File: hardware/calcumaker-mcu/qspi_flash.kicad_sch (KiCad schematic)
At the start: 3 parts, among them U7 W25Q32JVSSIQ

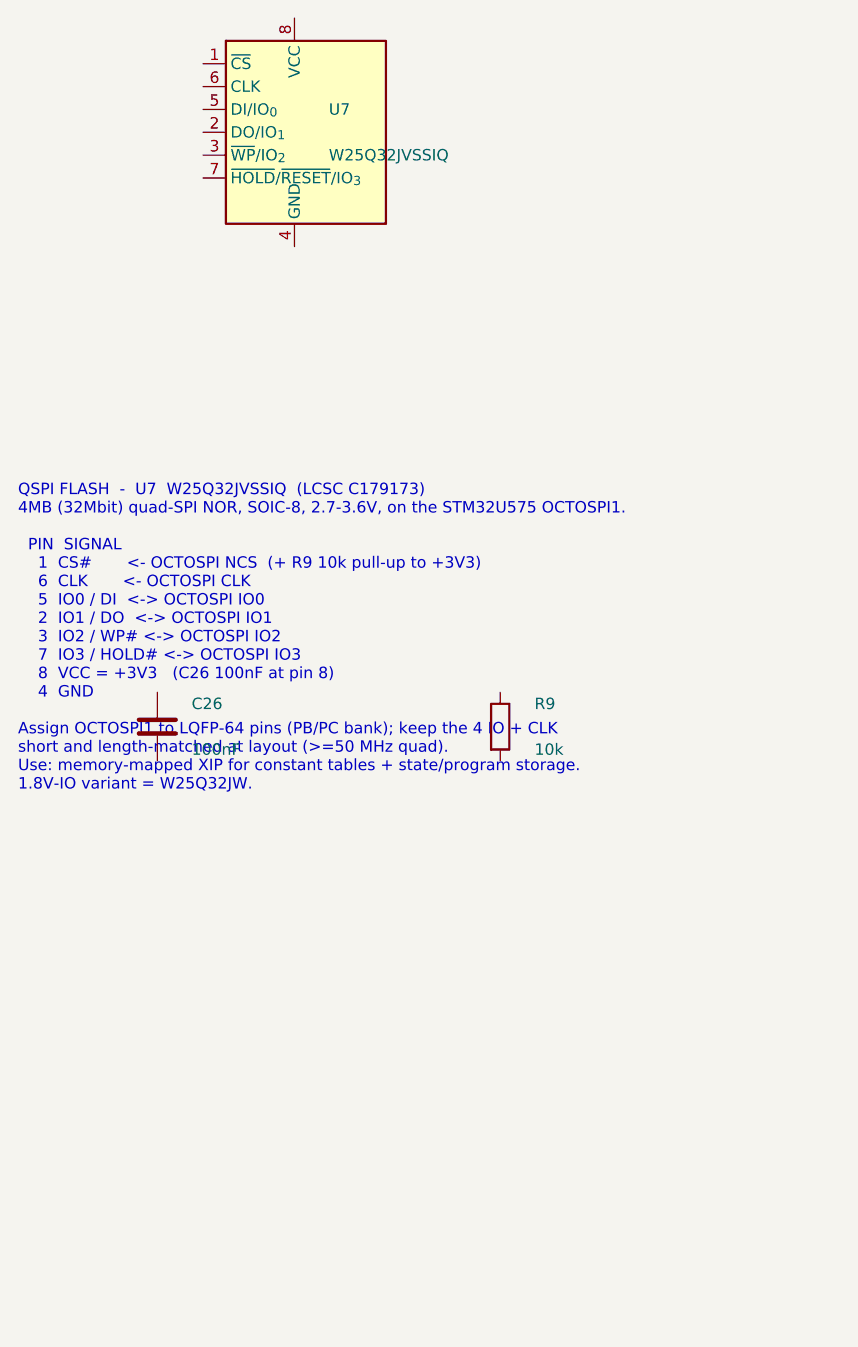
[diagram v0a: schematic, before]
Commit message: hardware: per-key RGB hint lighting on the keyboard board (50x SK6805 on gated VSYS) (#4)
Add addressable RGB accent lighting that hints key positions / presses -- one
SK6805-EC15 (1.5x1.5mm, the smallest serial RGB with a KiCad footprint + real
LCSC stock, C2890035) beside each of the 50 keys, single-wire daisy chain off
one STM32G0 pin.

Power: the LEDs are ~5V parts and the keyboard rail is only 3.3V, so they run
off VSYS (the MCU board's load-shared battery/USB rail, ~3.7-4.7V) brought up a
WIDENED 12-pin mezzanine (10 -> 12: +VSYS +GND). A high-side P-FET load switch
(Q1 AO3401A + Q2 2N7002) gates the whole LED rail off in sleep (G0 LED_EN) to
protect battery life, and a 74LVC1G125 (powered from the gated rail) level-shifts
the 3.3V data up to the LED VIH.

- calcumaker-keyboard: new KeyLighting sheet (50x SK6805 D56-D105 + U2 shifter +
  Q1/Q2 load switch + R7-R10 / C6-C7); J1 mezzanine -> 12-pin DF40C-12DP
  (C6224952). 119 -> 178 components.
- calcumaker-mcu: J5 mezzanine -> 12-pin DF40B-12DS (C3641147); route VSYS.
- DF40 stack: the receptacle SUFFIX sets the mated height (none = 1.5mm,
  (2.0) = 2.0mm, H-series = 2.5-4.0mm), NOT the B/C letter; the DF40C plug is the
  common header -- so DF40C-12DP x DF40B-12DS is a valid 1.5mm stack, same as the
  original 10-pin (DF40C-12DS just isn't LCSC-stocked).
- DESIGN.md / PARTS.md / memory: RGB subsystem, 12-pin pinout, BOM rows, the
  sleep-gate + current-cap notes (firmware must cap total brightness; 50x
  full-white ~0.75A would exceed the DF40 / VSYS budget).

All three boards regenerate + pass the structure check (mcu 55 / keyboard 178 /
display 60, no duplicate refs).

Co-authored-by: Claude Opus 4.8 (1M context) <noreply@anthropic.com>
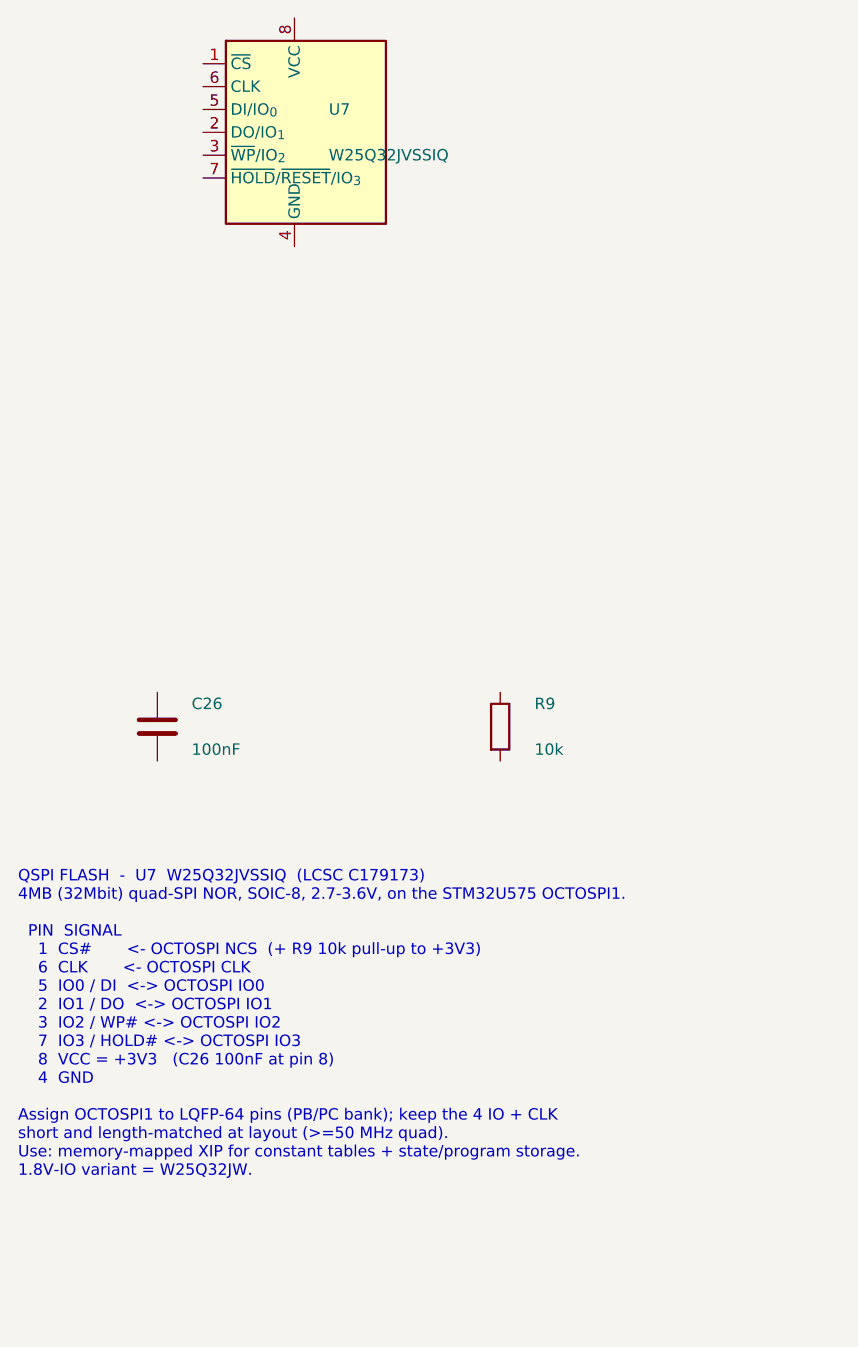
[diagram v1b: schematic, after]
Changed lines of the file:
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@@
 	(text "QSPI FLASH  -  U7  W25Q32JVSSIQ  (LCSC C179173)\n4MB (32Mbit) quad-SPI NOR, SOIC-8, 2.7-3.6V, on the STM32U575 OCTOSPI1.\n\n  PIN  SIGNAL                                              \n    1  CS#       <- OCTOSPI NCS  (+ R9 10k pull-up to +3V3)\n    6  CLK       <- OCTOSPI CLK                            \n    5  IO0 / DI  <-> OCTOSPI IO0                           \n    2  IO1 / DO  <-> OCTOSPI IO1                           \n    3  IO2 / WP# <-> OCTOSPI IO2                           \n    7  IO3 / HOLD# <-> OCTOSPI IO3                         \n    8  VCC = +3V3   (C26 100nF at pin 8)                   \n    4  GND\n\nAssign OCTOSPI1 to LQFP-64 pins (PB/PC bank); keep the 4 IO + CLK\nshort and length-matched at layout (>=50 MHz quad).\nUse: memory-mapped XIP for constant tables + state/program storage.\n1.8V-IO variant = W25Q32JW."
 		(exclude_from_sim no)
-		(at 15.00 95.00 0)
+		(at 15.00 137.92 0)
 		(effects (font (face "Courier New") (size 1.27 1.27)) (justify left top))
 	)

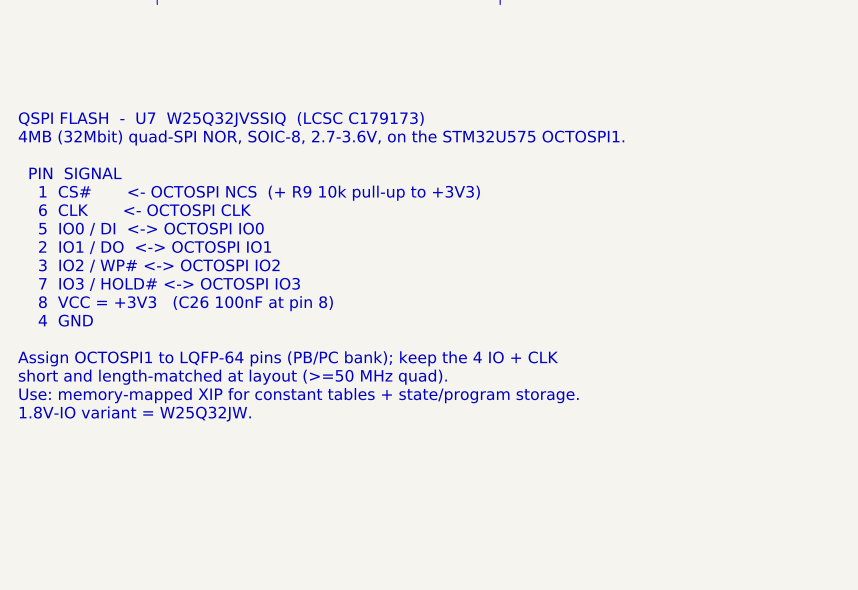
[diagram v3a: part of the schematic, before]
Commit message: hw: assign the OCTOSPI1 pinout and fold Clock/Prog/DisplayIF into MCU
The MCU sheet carried a "verify OCTOSPI1 pin mapping is available on
LQFP-64" TODO and the flash sheet said to assign it "to the PB/PC bank".
Both are now settled, and the PB/PC hint was wrong.

On the U5 the OCTOSPI GPIOs belong to the OCTOSPI I/O manager, so the AF
signals are OCTOSPIM_P1_*/P2_*. LQFP-64 bonds out no Port-2 bus at all
(ports E/F/G absent; only P2_NCS is present), so Port 1 is mandatory —
and on Port 1 IO0..IO3 each have exactly one candidate pin. Only CLK
(PA3|PB10) and NCS (PA2|PA4|PC11) were a real choice:

  CLK PB10 AF10 p29   IO0 PB1 AF10 p27   IO2 PA7 AF10 p23
  NCS PA4  AF3  p20   IO1 PB0 AF10 p26   IO3 PA6 AF10 p22

PB10+PA4 keep the whole bus in a contiguous pin 20-29 cluster (short and
length-matchable for >=50 MHz quad) and leave PA2/PA3 whole as the USART2
TX/RX pair for the keyboard link. It costs SPI1_NSS and WKUP2, both of
which have alternates. Every pin is verified against ST's package-filtered
CubeMX pin database for STM32U575RGTx / LQFP-64.

Taking PA6/PA7 for the flash consumes SPI1_MISO/MOSI, so the display
module bus moves to SCK=PA5, MOSI=PB5, CS=PA15. No MISO is needed — the
12-pin FFC doesn't carry one.

Sheet surgery: Clock (Y1 + C24/C25), Programming (J4) and DisplayIF
(J3 + J7) were already merged into the MCU sheet, leaving three files
unreferenced from the root. Delete them. The notes were edited in place
rather than regenerated, so the manual eeschema wiring survives; the
structure check reports the same 46 components and the same ERC tally as
before the change.

Also fix two things DESIGN.md got wrong on the way past:
  - The Power Tree still showed a 5V boost gated by DISP_PWR_EN and a
    74HCT125 on the MCU board. Those parts live on the display module now
    (DESIGN.md says so elsewhere) and exist on no sheet here; the PSU has
    only the TPS63900. VSYS passes through raw to J3/J7.
  - The board is 46 components, not 55.

Still open: KB_IRQ 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
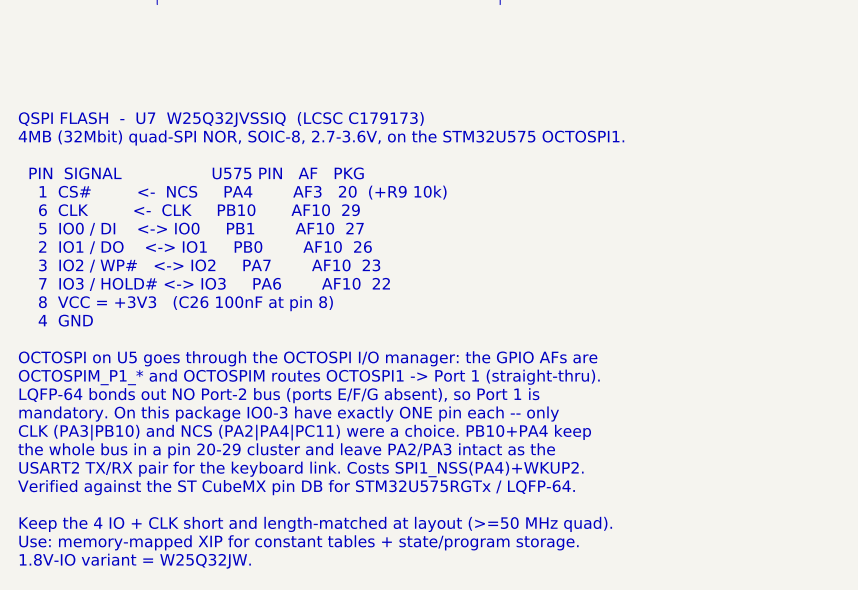
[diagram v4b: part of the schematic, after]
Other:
- note added: "QSPI FLASH - U7 W25Q32JVSSIQ (LCSC C179173) 4MB (32Mbit) quad-SPI NOR, SOIC-8, 2.7-3.6V, on the STM32U575 OCTOSPI1. PIN SIGNAL U575 PIN AF PKG 1 CS# <- NCS PA4 AF3 20 (+R9 10k) 6 CLK <- CLK PB10 AF10 29 5 IO0 / DI <-> IO0 PB1 AF10 27 2 IO1 / DO <-> IO1 PB0 AF10 26 3 IO2 / WP# <-> IO2 PA7 AF10 23 7 IO3 / HOLD# <-> IO3 PA6 AF10 22 8 VCC = +3V3 (C26 100nF at pin 8) 4 GND OCTOSPI on U5 goes through t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"
- note removed: "QSPI FLASH - U7 W25Q32JVSSIQ (LCSC C179173) 4MB (32Mbit) quad-SPI NOR, SOIC-8, 2.7-3.6V, on the STM32U575 OCTOSPI1. PIN SIGNAL 1 CS# <- OCTOSPI NCS (+ R9 10k pull-up to +3V3) 6 CLK <- OCTOSPI CLK 5 IO0 / DI <-> OCTOSPI IO0 2 IO1 / DO <-> OCTOSPI IO1 3 IO2 / WP# <-> OCTOSPI IO2 7 IO3 / HOLD# <-> OCTOSPI IO3 8 VCC = +3V3 (C26 100nF at pin 8) 4 GND Assign OCTOSPI1 to LQFP-64 pins (PB/PC bank); keep 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"
